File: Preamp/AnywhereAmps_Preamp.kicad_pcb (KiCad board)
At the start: 2 copper layers, 69.1 x 45.2 mm, 59 parts, among them J1 +9V, J2 Battery, J3 VCC, J4 Switch, J5 Pwr LED, J6 POTI, J7 Audio_In, J8 Audio_Out, U1 PTPSM5601R5H, U2 MAX17562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

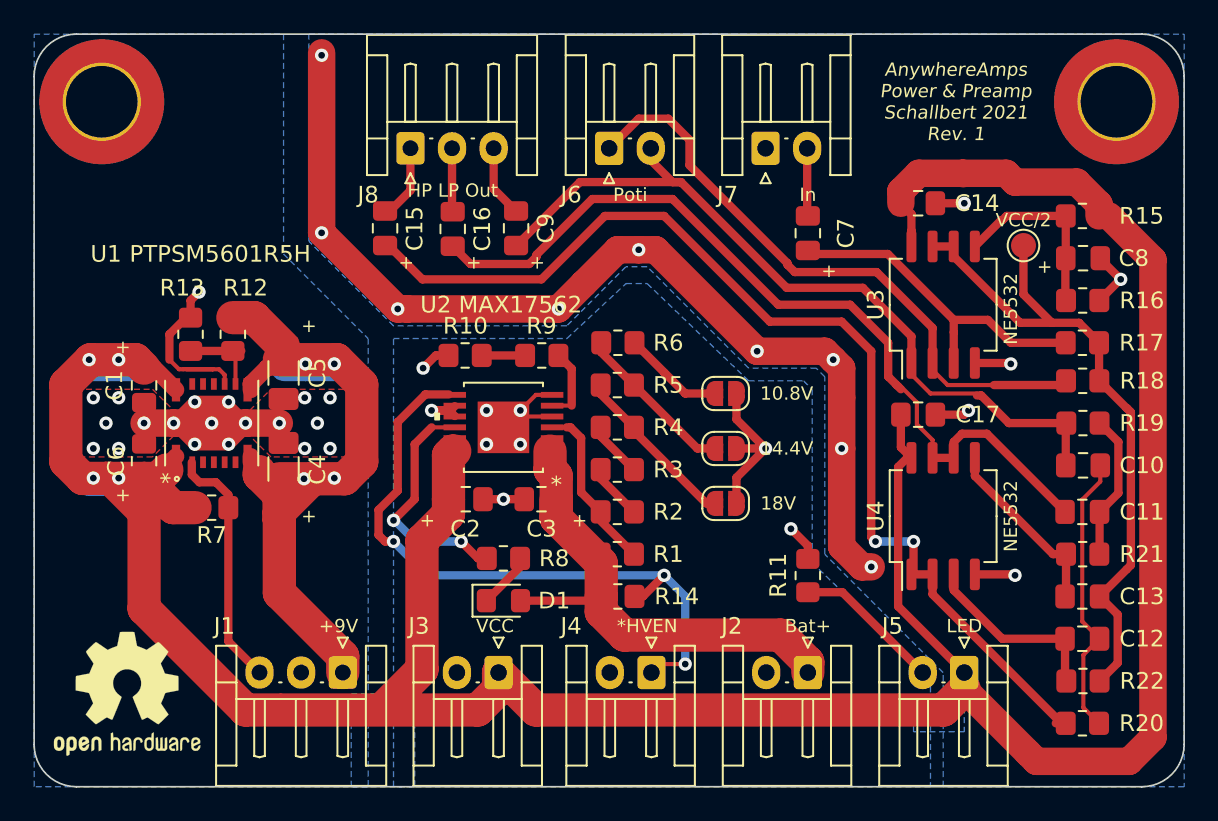
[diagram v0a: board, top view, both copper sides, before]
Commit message: - Change from EH to XH connectors, vertical - Re-align and place connectors - Delete LED, use TestPoint instead - Optimize 2mm tracks for shortness - update BOM
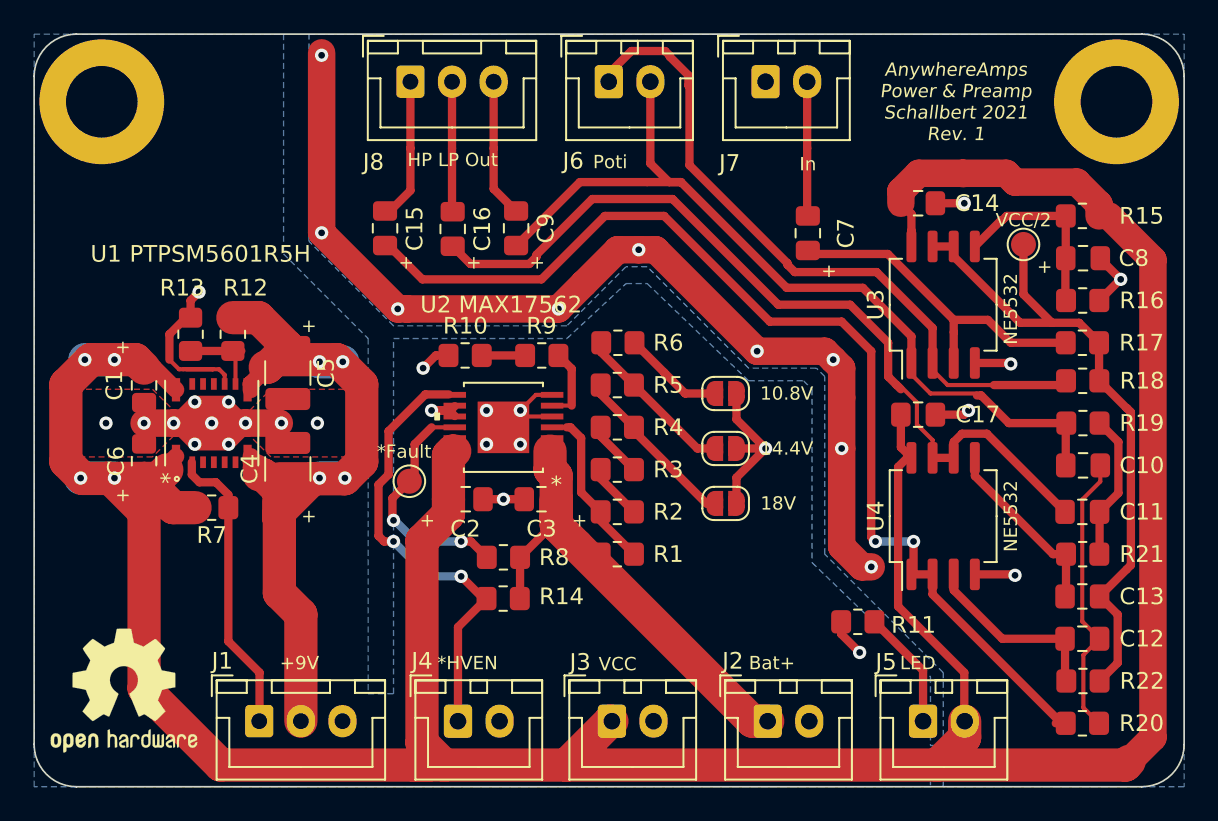
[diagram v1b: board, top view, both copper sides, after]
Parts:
- removed D1: Fault, LED_SMD:LED_0805_2012Metric_Pad1.15x1.40mm_HandSolder
- removed the REF** at (166.4, 105.7)
- removed the REF** at (105.4, 105.7)
- added REF**: MountingHole_4.3mm_M4_DIN965_Pad, MountingHole:MountingHole_4.3mm_M4_DIN965_Pad, F.Cu at (166.4, 105.7)
- added REF**: MountingHole_4.3mm_M4_DIN965_Pad, MountingHole:MountingHole_4.3mm_M4_DIN965_Pad, F.Cu at (105.4, 105.7)
- added TP2: TestPoint, TestPoint:TestPoint_Pad_D1.5mm, F.Cu at (160.8, 114.2)
- C4, C5: footprint Capacitor_SMD:C_1206_3216Metric_Pad1.33x1.80mm_HandSolder -> Capacitor_SMD:C_1210_3225Metric_Pad1.33x2.70mm_HandSolder
- J1, J8: footprint Connector_JST:JST_EH_S3B-EH_1x03_P2.50mm_Horizontal -> Connector_JST:JST_XH_B3B-XH-A_1x03_P2.50mm_Vertical
- J2, J3, J4, J5, J6, J7: footprint Connector_JST:JST_EH_S2B-EH_1x02_P2.50mm_Horizontal -> Connector_JST:JST_XH_B2B-XH-A_1x02_P2.50mm_Vertical
- R8: value 1.25k -> 390k
- TP1: value TestPoint -> *Fault
- moved TP1 39.5 mm to (123.9, 128.5)
- moved J4 12.0 mm to (126.8, 142.9), turned to 0 degrees
- moved J3 7.41 mm to (136.1, 142.9), turned to 0 degrees
- moved R14 6.89 mm to (129.5, 135.5), turned to 0 degrees
- moved J1 5.80 mm to (114.9, 142.9), turned to 0 degrees
- moved R11 4.09 mm to (150.8, 136.9), turned to 0 degrees
- moved J6 4.00 mm to (135.9, 104.5)
- moved J7 4.00 mm to (145.3, 104.5)
- moved J8 4.00 mm to (124.0, 104.5)
- moved J5 3.83 mm to (154.7, 142.9), turned to 0 degrees
- moved J2 3.79 mm to (145.4, 142.9), turned to 0 degrees
- moved REF** 0.27 mm to (106.7, 141.0)
- moved C4 0.25 mm to (116.6, 127.7)
- moved C5 0.25 mm to (116.6, 122.0)
- moved R8 0.06 mm to (129.5, 133.0)
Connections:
- J1 pad 1: +9V -> EN
- J1 pad 2: GND -> +9V
- J1 pad 3: EN -> GND
- J5 pad 1: VCC -> Net-(J5-Pad1)
- J5 pad 2: Net-(J5-Pad2) -> VCC
- R11 pad 2: Net-(J5-Pad2) -> Net-(J5-Pad1)
- R8 pad 1: Net-(D1-Pad1) -> +BATT
- TP1 pad 1: GNDA -> *FLAG
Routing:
- net *HVEN: track 39.8 -> 27.2 mm, vias 3 -> 2
- net Net-(J5-Pad2): track 8.90 -> 0.00 mm
- net Net-(J5-Pad1): track 0.00 -> 8.00 mm
- net VCC: track 201.2 -> 208.9 mm
- net +9V: track 47.8 -> 52.4 mm
- net Poti: track 37.3 -> 41.6 mm
- net AudioOut: track 4.35 -> 8.35 mm
- net LP_Out: track 3.83 -> 7.83 mm
- net HP_Out: track 4.34 -> 8.34 mm
- net AudioIn: track 4.29 -> 8.29 mm
- net PreampOut: track 48.2 -> 51.7 mm
- net Net-(D1-Pad1): track 3.44 -> 0.00 mm
- net EN: track 15.0 -> 18.0 mm
- net +BATT: track 31.1 -> 29.5 mm
- net GND: track 136.8 -> 136.9 mm, vias 43 -> 35
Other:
- board text added: "*Fault"
- board text added: "33n MLCC C10, C11, C12, C13, C14, C17 4.7u low ESR Tantalum C1, C2, C3, C6, C7, C8, C9, C15, C16 47u low ESR Tantalum C4, C5 390k R1, R7, R8, R14 10k R2, R3, R4, R5, R6, R12, R15, R16, R17, R18, R19, R20, R21, R22 1.25k R9, R10, R11, R13"
- board text removed: "33n MLCC C10, C11, C12, C13, C14, C17 4.7u low ESR Tantalum C1, C2, C3, C6, C7, C8, C9, C15, C16 47u low ESR Tantalum C4, C5 390k R1, R7, R9, R15 10k R2, R3, R4, R5, R6, R13, R16, R17, R18, R19, R20, R21, R22, R23 1.25k R8, R10, R11, R12, R14"

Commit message: - improve via'd tracks - fix silkscreen items
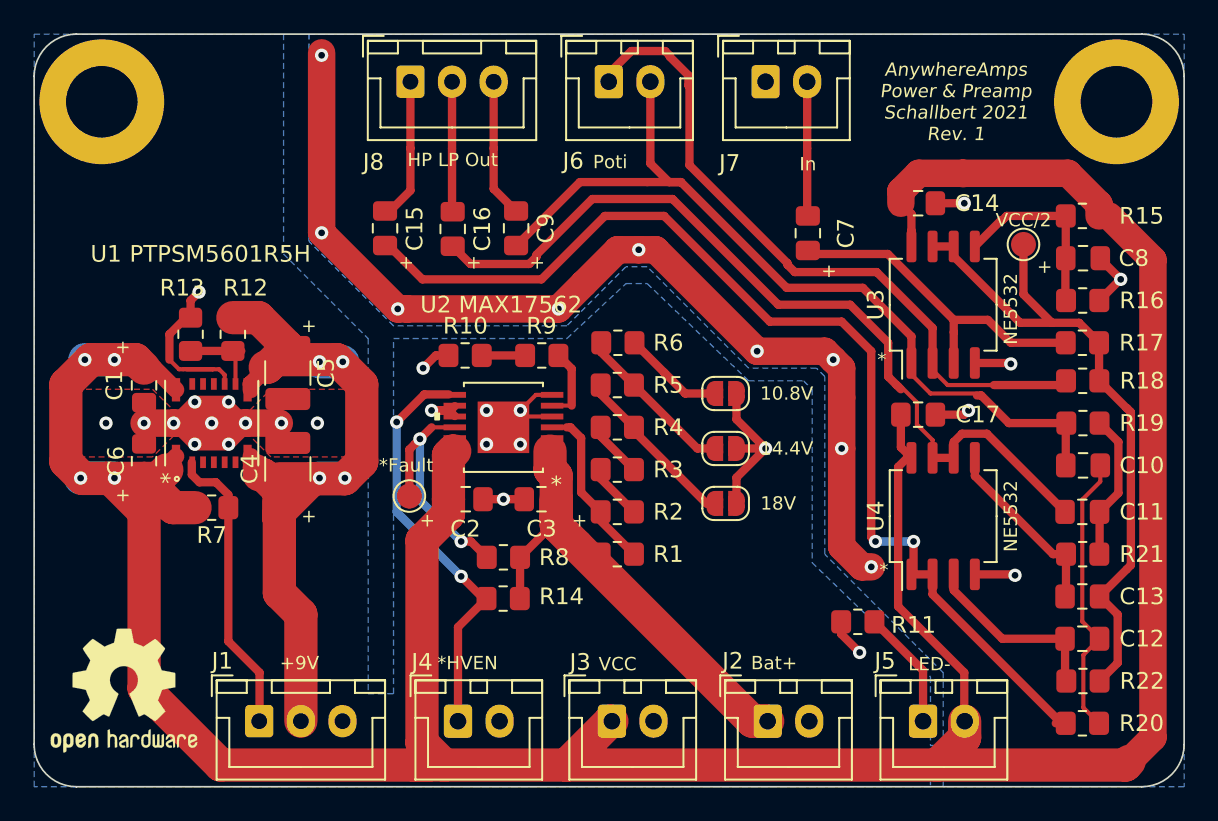
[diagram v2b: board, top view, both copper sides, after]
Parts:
- moved TP1 0.89 mm to (123.9, 129.3)
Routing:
- net *HVEN: track 27.2 -> 24.8 mm
- net *FLAG: track 15.1 -> 15.7 mm
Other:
- board text added: "*"
- board text added: "LED-"
- board text removed: "LED"
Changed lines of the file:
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@@
   (general
     (thickness 1.6002)
-    (drawings 39)
-    (tracks 475)
+    (drawings 41)
+    (tracks 462)
     (zones 0)
     (modules 59)
@@
     (descr "JST XH series connector, B2B-XH-A (http://www.jst-mfg.com/product/pdf/eng/eXH.pdf), generated with kicad-footprint-generator")
     (tags "connector JST XH vertical")
-    (fp_text reference J5 (at -2.2225 -3.556) (layer F.SilkS)
+    (fp_text reference J5 (at -2.286 -3.6195) (layer F.SilkS)
       (effects (font (size 1 1) (thickness 0.15)))
     )
@@
     (descr "JST XH series connector, B2B-XH-A (http://www.jst-mfg.com/product/pdf/eng/eXH.pdf), generated with kicad-footprint-generator")
     (tags "connector JST XH vertical")
-    (fp_text reference J4 (at -2.159 -3.6195) (layer F.SilkS)
+    (fp_text reference J4 (at -2.159 -3.556) (layer F.SilkS)
       (effects (font (size 1 1) (thickness 0.15)))
     )
@@
   )
   (module TestPoint:TestPoint_Pad_D1.5mm (layer Front)
-    (at 123.8885 128.4605)
+    (at 123.8885 129.3495)
     (descr "SMD pad as test Point, diameter 1.5mm")
     (tags "test point SMD pad")
@@
     )
   )
-  (gr_text *Fault (at 123.571 126.6825) (layer F.SilkS)
+  (gr_text * (at 152.273 121.158) (layer F.SilkS)
+    (effects (font (size 0.8 0.8) (thickness 0.1)))
+  )
+  (gr_text * (at 152.4 133.7945) (layer F.SilkS)
+    (effects (font (size 0.8 0.8) (thickness 0.1)))
+  )
+  (gr_text *Fault (at 123.698 127.508) (layer F.SilkS)
     (effects (font (size 0.8 0.8) (thickness 0.1)))
   )
@@
     (effects (font (size 0.8 0.8) (thickness 0.1)))
   )
-  (gr_text "LED\n" (at 154.432 139.3825) (layer F.SilkS)
+  (gr_text LED- (at 155.1305 139.446) (layer F.SilkS)
     (effects (font (size 0.8 0.8) (thickness 0.1)))
   )
-  (gr_text "Bat+\n" (at 145.669 139.3825) (layer F.SilkS)
+  (gr_text "Bat+\n" (at 145.796 139.3825) (layer F.SilkS)
     (effects (font (size 0.8 0.8) (thickness 0.1)))
   )
@@
   (segment (start 168.55953 115.15953) (end 168.55953 143.86047) (width 1.65) (layer Front) (net 1))
   (segment (start 165.922 112.522) (end 168.55953 115.15953) (width 1.65) (layer Front) (net 1))
-  (segment (start 165.322 112.522) (end 165.322 111.822) (width 1.65) (layer Front) (net 1))
-  (segment (start 157.13934 109.95999) (end 159.74399 109.95999) (width 1.65) (layer Front) (net 1))
-  (segment (start 159.74399 109.95999) (end 160.274 110.49) (width 1.65) (layer Front) (net 1))
-  (segment (start 163.99 110.49) (end 165.322 111.822) (width 1.65) (layer Front) (net 1))
-  (segment (start 160.274 110.49) (end 163.99 110.49) (width 1.65) (layer Front) (net 1))
   (segment (start 109.7065 130.048) (end 111.014 130.048) (width 2) (layer Front) (net 1))
   (segment (start 107.95 128.2915) (end 109.7065 130.048) (width 2) (layer Front) (net 1))
@@
   (segment (start 104.394 121.158) (end 106.172 121.158) (width 2) (layer Back) (net 1))
   (segment (start 104.14 128.27) (end 106.172 128.27) (width 2) (layer Back) (net 1))
+  (segment (start 165.322 111.822) (end 165.322 112.522) (width 1.65) (layer Front) (net 1))
+  (segment (start 163.45999 109.95999) (end 165.322 111.822) (width 1.65) (layer Front) (net 1))
+  (segment (start 157.13934 109.95999) (end 163.45999 109.95999) (width 1.65) (layer Front) (net 1))
   (via (at 118.618 102.87) (size 0.8) (drill 0.4) (layers Front Back) (net 2))
   (via (at 151.638 133.604) (size 0.8) (drill 0.4) (layers Front Back) (net 2))
@@
   (segment (start 126.452 108.458) (end 126.452 112.228) (width 0.5) (layer Front) (net 16))
   (via (at 127 134.1755) (size 0.8) (drill 0.4) (layers Front Back) (net 17))
-  (via (at 122.936 132.08) (size 0.8) (drill 0.4) (layers Front Back) (net 17))
+  (via (at 123.1265 124.9045) (size 0.8) (drill 0.4) (layers Front Back) (net 17))
   (segment (start 137.414 135.382) (end 137.668 135.382) (width 0.25) (layer Front) (net 3))
   (segment (start 137.414 135.382) (end 137.922 135.382) (width 0.5) (layer Front) (net 3))
@@
   (segment (start 123.952 108.458) (end 123.952 104.4575) (width 0.5) (layer Front) (net 15))
   (segment (start 126.452 108.458) (end 126.452 104.4575) (width 0.5) (layer Front) (net 16))
-  (segment (start 122.370315 132.08) (end 122.936 132.08) (width 0.5) (layer Front) (net 17))
-  (segment (start 122.035999 131.745684) (end 122.370315 132.08) (width 0.5) (layer Front) (net 17))
-  (segment (start 122.035999 128.662001) (end 122.035999 131.745684) (width 0.5) (layer Front) (net 17))
-  (segment (start 122.638499 128.059501) (end 122.035999 128.662001) (width 0.5) (layer Front) (net 17))
-  (segment (start 122.638499 125.457499) (end 122.638499 128.059501) (width 0.5) (layer Front) (net 17))
-  (segment (start 124.851399 123.244599) (end 122.638499 125.457499) (width 0.5) (layer Front) (net 17))
-  (segment (start 126.259579 123.244599) (end 124.851399 123.244599) (width 0.5) (layer Front) (net 17))
   (segment (start 126.8095 137.2235) (end 126.8095 142.875) (width 0.5) (layer Front) (net 17))
   (segment (start 128.524 135.509) (end 126.8095 137.2235) (width 0.5) (layer Front) (net 17))
   (segment (start 128.3335 135.509) (end 127 134.1755) (width 0.5) (layer Front) (net 17))
   (segment (start 128.524 135.509) (end 128.3335 135.509) (width 0.5) (layer Front) (net 17))
-  (segment (start 125.0315 134.1755) (end 127 134.1755) (width 0.5) (layer Back) (net 17))
-  (segment (start 122.936 132.08) (end 125.0315 134.1755) (width 0.5) (layer Back) (net 17))
+  (segment (start 124.786401 123.244599) (end 123.1265 124.9045) (width 0.5) (layer Front) (net 17))
+  (segment (start 126.259579 123.244599) (end 124.786401 123.244599) (width 0.5) (layer Front) (net 17))
+  (segment (start 123.1265 130.302) (end 123.1265 124.9045) (width 0.5) (layer Back) (net 17))
+  (segment (start 127 134.1755) (end 123.1265 130.302) (width 0.5) (layer Back) (net 17))
   (segment (start 155.321 121.778478) (end 156.224522 122.682) (width 0.25) (layer Front) (net 18))
   (segment (start 155.321 121.356) (end 155.321 121.778478) (width 0.25) (layer Front) (net 18))
@@
   (segment (start 134.21001 125.863409) (end 133.568601 125.222) (width 0.5) (layer Front) (net 23))
   (segment (start 133.568601 125.222) (end 133.343601 125.222) (width 0.5) (layer Front) (net 23))
-  (via (at 127 132.08) (size 0.8) (drill 0.4) (layers Front Back) (net 24))
   (segment (start 126.615452 125.222) (end 125.222 125.222) (width 0.25) (layer Front) (net 24))
-  (segment (start 123.060051 130.685949) (end 122.936 130.81) (width 0.25) (layer Front) (net 24))
-  (via (at 122.936 130.81) (size 0.8) (drill 0.4) (layers Front Back) (net 24))
-  (segment (start 122.936 130.81) (end 122.998002 130.81) (width 0.5) (layer Back) (net 24))
-  (segment (start 124.268002 132.08) (end 127 132.08) (width 0.5) (layer Back) (net 24))
-  (segment (start 122.998002 130.81) (end 124.268002 132.08) (width 0.5) (layer Back) (net 24))
   (segment (start 125.222 125.222) (end 124.206 126.238) (width 0.5) (layer Front) (net 24))
-  (segment (start 123.8885 128.4605) (end 124.0155 128.4605) (width 0.5) (layer Front) (net 24))
-  (segment (start 124.0155 128.4605) (end 124.206 128.27) (width 0.5) (layer Front) (net 24))
-  (segment (start 124.206 128.143) (end 123.8885 128.4605) (width 0.5) (layer Front) (net 24))
-  (segment (start 124.206 126.238) (end 124.206 128.143) (width 0.5) (layer Front) (net 24))
-  (segment (start 123.8885 128.4605) (end 122.8725 129.4765) (width 0.5) (layer Front) (net 24))
-  (segment (start 122.8725 130.7465) (end 122.936 130.81) (width 0.5) (layer Front) (net 24))
-  (segment (start 122.8725 129.4765) (end 122.8725 130.7465) (width 0.5) (layer Front) (net 24))
+  (segment (start 123.8885 126.5555) (end 124.206 126.238) (width 0.5) (layer Front) (net 24))
+  (segment (start 123.8885 129.3495) (end 123.8885 126.5555) (width 0.5) (layer Front) (net 24))
+  (segment (start 123.8885 129.3495) (end 123.8885 129.8575) (width 0.5) (layer Front) (net 24))
+  (via (at 127 132.08) (size 0.8) (drill 0.4) (layers Front Back) (net 24))
   (segment (start 127.5875 132.08) (end 128.54 133.0325) (width 0.5) (layer Front) (net 24))
   (segment (start 127 132.08) (end 127.5875 132.08) (width 0.5) (layer Front) (net 24))
+  (via (at 124.5235 125.9205) (size 0.8) (drill 0.4) (layers Front Back) (net 24))
+  (segment (start 124.5235 129.6035) (end 127 132.08) (width 0.5) (layer Back) (net 24))
+  (segment (start 124.5235 125.9205) (end 124.5235 129.6035) (width 0.5) (layer Back) (net 24))
   (segment (start 110.744 127.418) (end 110.844 127.318) (width 0.25) (layer Front) (net 32))
   (segment (start 113.014 130.048) (end 113.014 129.27) (width 0.5) (layer Front) (net 32))
